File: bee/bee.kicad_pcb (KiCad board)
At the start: 2 copper layers, 29 x 53.3 mm, 12 parts, among them J1 Conn_01x02_Male, J2 Conn_01x02_Male, J3 Conn_01x02_Male, J4 Conn_01x02_Male

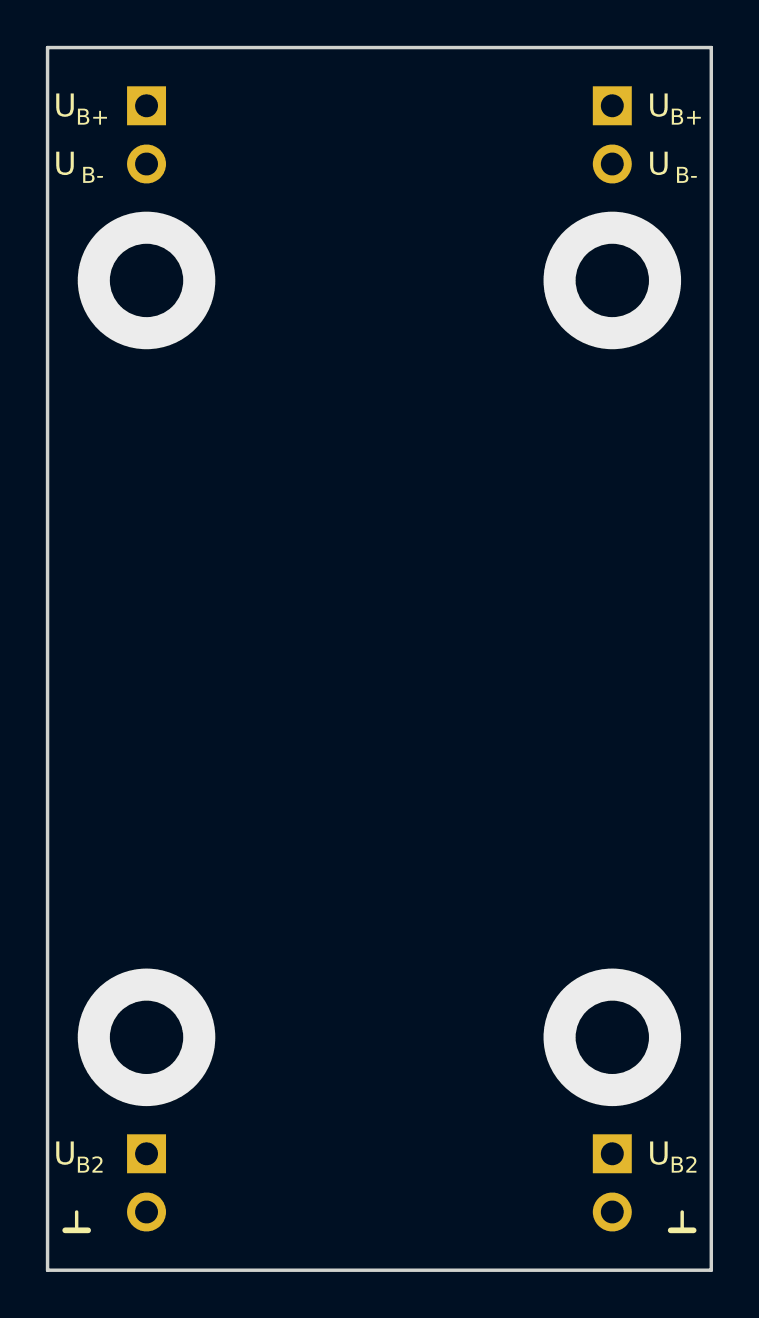
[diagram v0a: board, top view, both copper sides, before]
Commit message: Replace vias by mounting holes.
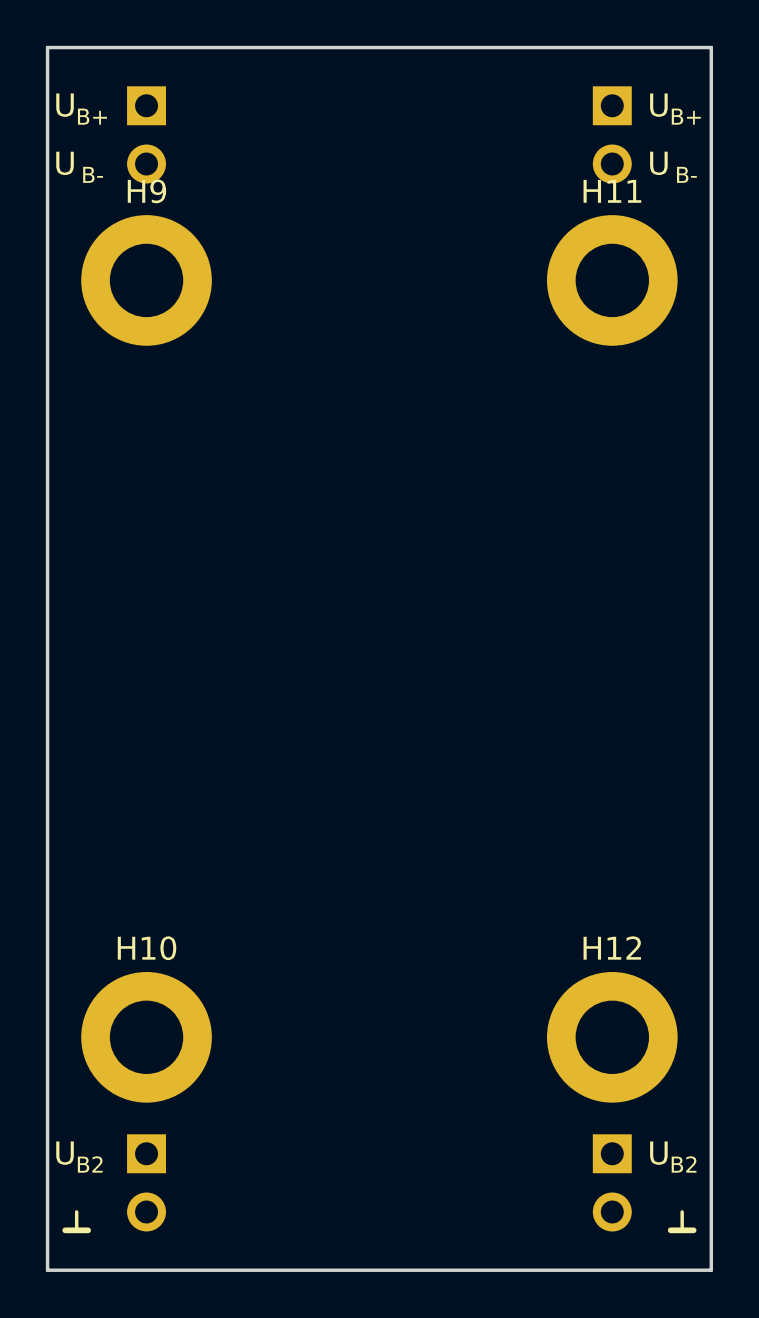
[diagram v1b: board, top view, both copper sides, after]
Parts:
- added H10: MountingHole_Pad, MountingHole:MountingHole_3.2mm_M3_ISO7380_Pad, F.Cu at (78.7, 132.1)
- added H11: MountingHole_Pad, MountingHole:MountingHole_3.2mm_M3_ISO7380_Pad, F.Cu at (99.1, 99.1)
- added H12: MountingHole_Pad, MountingHole:MountingHole_3.2mm_M3_ISO7380_Pad, F.Cu at (99.1, 132.1)
- added H9: MountingHole_Pad, MountingHole:MountingHole_3.2mm_M3_ISO7380_Pad, F.Cu at (78.7, 99.1)
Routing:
- net (no net): vias 4 -> 0
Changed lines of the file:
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@@
     (thickness 1.6)
     (drawings 4)
-    (tracks 4)
+    (tracks 0)
     (zones 0)
-    (modules 12)
+    (modules 16)
     (nets 5)
   )
@@
     (fp_line (start -0.5 0.8) (end 0.5 0.8) (layer F.SilkS) (width 0.25))
   )
+  (module MountingHole:MountingHole_3.2mm_M3_ISO7380_Pad locked (layer F.Cu)
+    (at 78.74 99.06)
+    (descr "Mounting Hole 3.2mm, M3, ISO7380")
+    (tags "mounting hole 3.2mm m3 iso7380")
+    (attr virtual)
+    (fp_text reference H9 (at 0 -3.85) (layer F.SilkS)
+      (effects (font (size 1 1) (thickness 0.15)))
+    )
+    (fp_text value MountingHole_Pad (at 0 3.85) (layer F.Fab)
+      (effects (font (size 1 1) (thickness 0.15)))
+    )
+    (fp_text user %R (at 0.3 0) (layer F.Fab)
+      (effects (font (size 1 1) (thickness 0.15)))
+    )
+    (fp_circle (center 0 0) (end 2.85 0) (layer Cmts.User) (width 0.15))
+    (fp_circle (center 0 0) (end 3.1 0) (layer F.CrtYd) (width 0.05))
+    (pad 1 thru_hole circle (at 0 0) (size 5.7 5.7) (drill 3.2) (layers *.Cu *.Mask)
+      (net 3 GND))
+  )
+  (module MountingHole:MountingHole_3.2mm_M3_ISO7380_Pad locked (layer F.Cu)
+    (at 78.74 132.08)
+    (descr "Mounting Hole 3.2mm, M3, ISO7380")
+    (tags "mounting hole 3.2mm m3 iso7380")
+    (attr virtual)
+    (fp_text reference H10 (at 0 -3.85) (layer F.SilkS)
+      (effects (font (size 1 1) (thickness 0.15)))
+    )
+    (fp_text value MountingHole_Pad (at 0 3.85) (layer F.Fab)
+      (effects (font (size 1 1) (thickness 0.15)))
+    )
+    (fp_text user %R (at 0.3 0) (layer F.Fab)
+      (effects (font (size 1 1) (thickness 0.15)))
+    )
+    (fp_circle (center 0 0) (end 2.85 0) (layer Cmts.User) (width 0.15))
+    (fp_circle (center 0 0) (end 3.1 0) (layer F.CrtYd) (width 0.05))
+    (pad 1 thru_hole circle (at 0 0) (size 5.7 5.7) (drill 3.2) (layers *.Cu *.Mask)
+      (net 3 GND))
+  )
+  (module MountingHole:MountingHole_3.2mm_M3_ISO7380_Pad locked (layer F.Cu)
+    (at 99.06 99.06)
+    (descr "Mounting Hole 3.2mm, M3, ISO7380")
+    (tags "mounting hole 3.2mm m3 iso7380")
+    (attr virtual)
+    (fp_text reference H11 (at 0 -3.85) (layer F.SilkS)
+      (effects (font (size 1 1) (thickness 0.15)))
+    )
+    (fp_text value MountingHole_Pad (at 0 3.85) (layer F.Fab)
+      (effects (font (size 1 1) (thickness 0.15)))
+    )
+    (fp_circle (center 0 0) (end 3.1 0) (layer F.CrtYd) (width 0.05))
+    (fp_circle (center 0 0) (end 2.85 0) (layer Cmts.User) (width 0.15))
+    (fp_text user %R (at 0.3 0) (layer F.Fab)
+      (effects (font (size 1 1) (thickness 0.15)))
+    )
+    (pad 1 thru_hole circle (at 0 0) (size 5.7 5.7) (drill 3.2) (layers *.Cu *.Mask)
+      (net 3 GND))
+  )
+  (module MountingHole:MountingHole_3.2mm_M3_ISO7380_Pad locked (layer F.Cu)
+    (at 99.06 132.08)
+    (descr "Mounting Hole 3.2mm, M3, ISO7380")
+    (tags "mounting hole 3.2mm m3 iso7380")
+    (attr virtual)
+    (fp_text reference H12 (at 0 -3.85) (layer F.SilkS)
+      (effects (font (size 1 1) (thickness 0.15)))
+    )
+    (fp_text value MountingHole_Pad (at 0 3.85) (layer F.Fab)
+      (effects (font (size 1 1) (thickness 0.15)))
+    )
+    (fp_circle (center 0 0) (end 3.1 0) (layer F.CrtYd) (width 0.05))
+    (fp_circle (center 0 0) (end 2.85 0) (layer Cmts.User) (width 0.15))
+    (fp_text user %R (at 0.3 0) (layer F.Fab)
+      (effects (font (size 1 1) (thickness 0.15)))
+    )
+    (pad 1 thru_hole circle (at 0 0) (size 5.7 5.7) (drill 3.2) (layers *.Cu *.Mask)
+      (net 3 GND))
+  )
   (gr_line (start 103.378 88.9) (end 103.378 142.24) (layer Edge.Cuts) (width 0.15))
   (gr_line (start 74.422 142.24) (end 103.378 142.24) (layer Edge.Cuts) (width 0.15))
   (gr_line (start 74.422 88.9) (end 103.378 88.9) (layer Edge.Cuts) (width 0.15))
   (gr_line (start 74.422 88.9) (end 74.422 142.24) (layer Edge.Cuts) (width 0.15))
-  (via (at 78.74 99.06) (size 6) (drill 3.2) (layers F.Cu B.Cu) (net 0) (status 40000))
-  (via (at 99.06 99.06) (size 6) (drill 3.2) (layers F.Cu B.Cu) (net 0) (status 40000))
-  (via (at 99.06 132.08) (size 6) (drill 3.2) (layers F.Cu B.Cu) (net 0) (status 40000))
-  (via (at 78.74 132.08) (size 6) (drill 3.2) (layers F.Cu B.Cu) (net 0) (status 40000))
 )
